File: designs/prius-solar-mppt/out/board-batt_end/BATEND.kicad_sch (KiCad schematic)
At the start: 15 parts, among them J901 1766356, J902 1766343, J903 1757255, K901 G9KB-1A DC12, K902 G9KB-1A DC12

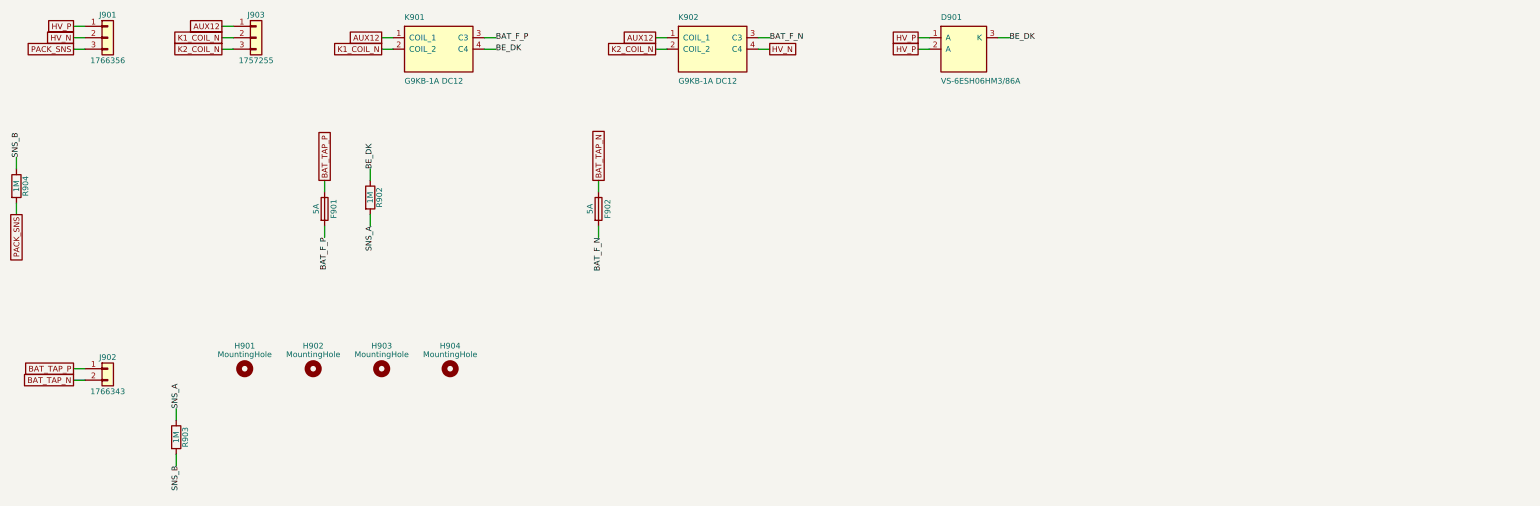
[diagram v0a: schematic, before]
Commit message: designs/prius-solar-mppt: v0.3, fix the independent review's blockers and majors
- B1: CHASSIS domain with reinforced DC barriers to HV and PACK (10/8 mm), HV/PACK edge
  clearance 10 mm, mounting holes fixed with 13 mm keep-outs; thermal pedestal under LV
  parts only.
- B2: no primary source for the Prime's full-charge cell voltage was found (blocking
  Q-13); hardware clamp set below a 4.00 V/cell floor (L3 3.927 V, worst 3.963 V; L2
  3.836 V; L1 3.79 V) with DNP trim to raise later; until then charging may stop near
  55-65 % SOC.
- Majors: sink clamp + burst disable + PV-node trip and TVS against LM5176 reverse power;
  20 MHz AEC-Q200 crystal for CAN (listen-only start); parked insulation monitoring via a
  110 M bridge (also detects a welded relay); open-sensor-safe hardware OT; CAGE CLAMP HV
  terminals with a lid-switch HVIL; DCX on-time and 17.6 A primary overcurrent latches;
  supercap-held latch that clears overnight.
- Build: 0 errors, ERC clean, system and both board netlists identical; 9 waivers (17
  findings, was 32).

Co-Authored-By: Claude Opus 5.5 <noreply@anthropic.com>
Claude-Session: https://claude.ai/code/session_01VFJn9VbX8h27kf4LpLwEtn
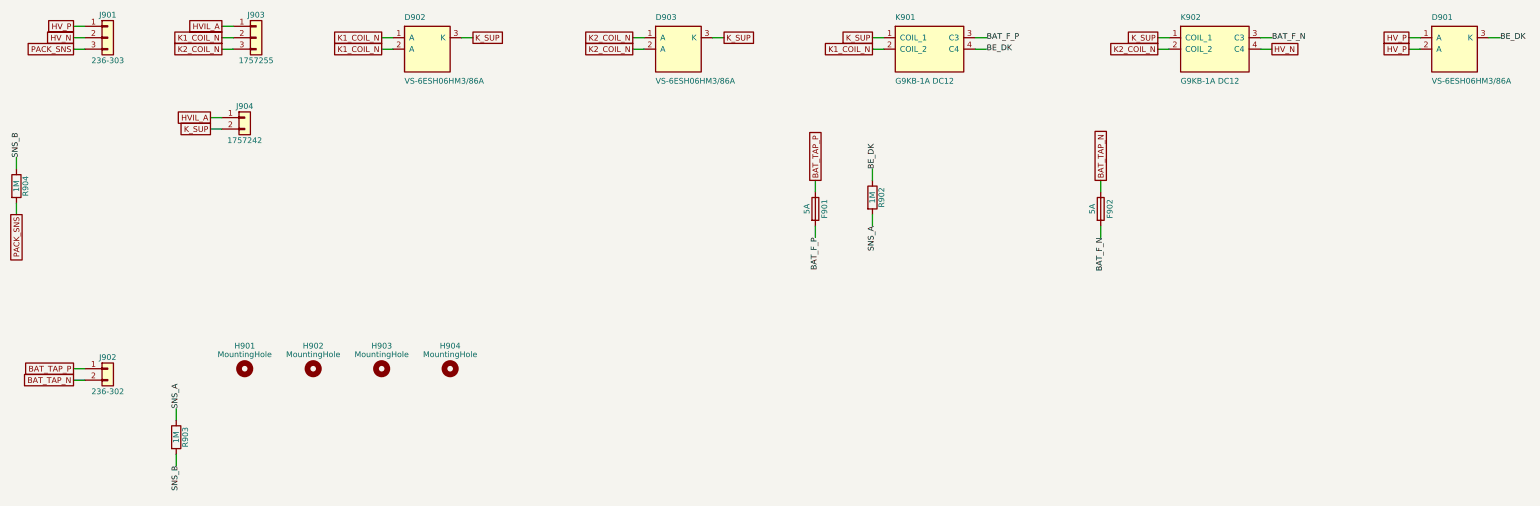
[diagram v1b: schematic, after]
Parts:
- added D902, D903: VS-6ESH06HM3/86A, Package_TO_SOT_SMD:TO-277A, symbol kaesynth:VS-6ESH06HM3_86A
- added J904: 1757242, Connector_Phoenix_MSTB:PhoenixContact_MSTBA_2,5_2-G-5,08_1x02_P5.08mm_Horizontal, symbol Connector_Generic:Conn_01x02
- J901: value 1766356 -> 236-303; footprint Connector_Phoenix_GMSTB:PhoenixContact_GMSTBA_2,5_3-G-7,62_1x03_P7.62mm_Horizontal -> TerminalBlock_WAGO:TerminalBlock_WAGO_236-303_1x03_P10.00mm_45Degree; MPN 1766356 -> 236-303; Manufacturer Phoenix Contact -> WAGO
- J902: value 1766343 -> 236-302; footprint Connector_Phoenix_GMSTB:PhoenixContact_GMSTBA_2,5_2-G-7,62_1x02_P7.62mm_Horizontal -> TerminalBlock_WAGO:TerminalBlock_WAGO_236-302_1x02_P10.00mm_45Degree; MPN 1766343 -> 236-302; Manufacturer Phoenix Contact -> WAGO
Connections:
- net K1_COIL_N: now also D902.1 (A), D902.2 (A)
- net K2_COIL_N: now also D903.1 (A), D903.2 (A)
- net AUX12 renamed K_SUP
- net K_SUP: now also D902.3 (K), D903.3 (K), J904.2 (Pin_2); no longer J903.1 (Pin_1)
- new net HVIL_A: J903.1 (Pin_1), J904.1 (Pin_1)
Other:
- moved on the sheet: D901, F901, F902, K901, K902, R902
